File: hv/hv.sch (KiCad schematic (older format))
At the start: 26 parts, among them P1 CONN_02X03, P10 CONN_01X01, P2 CONN_01X02, P3 CONN_01X01, P4 CONN_01X01, P5 CONN_01X01, P6 CONN_01X02, P7 CONN_01X01, P8 CONN_01X01, P9 CONN_01X01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

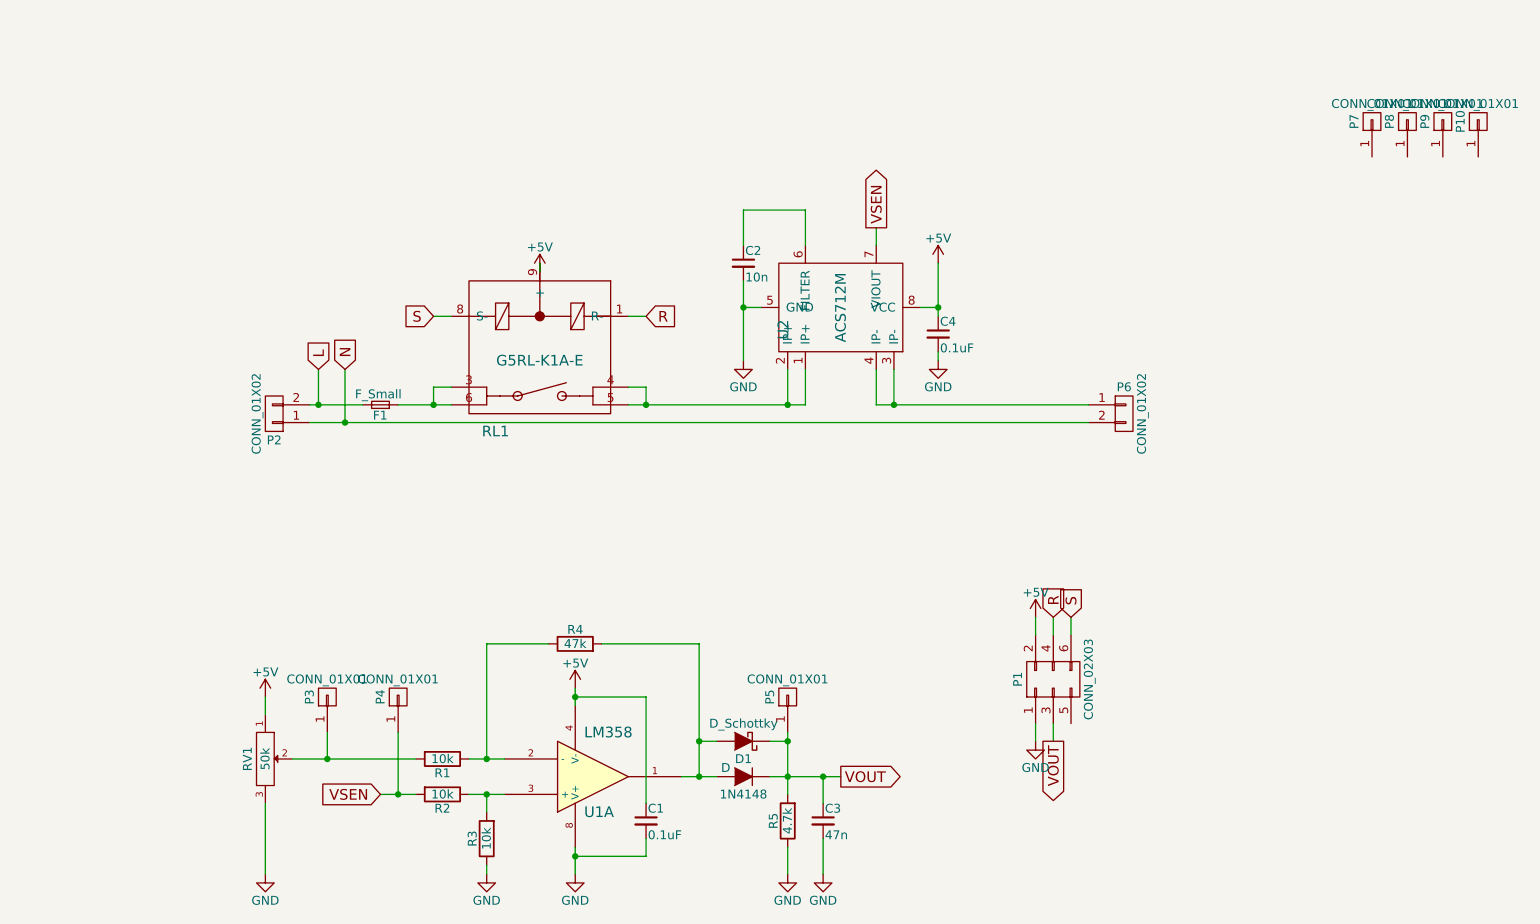
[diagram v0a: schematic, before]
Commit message: Rerouting on 5x5 cm2
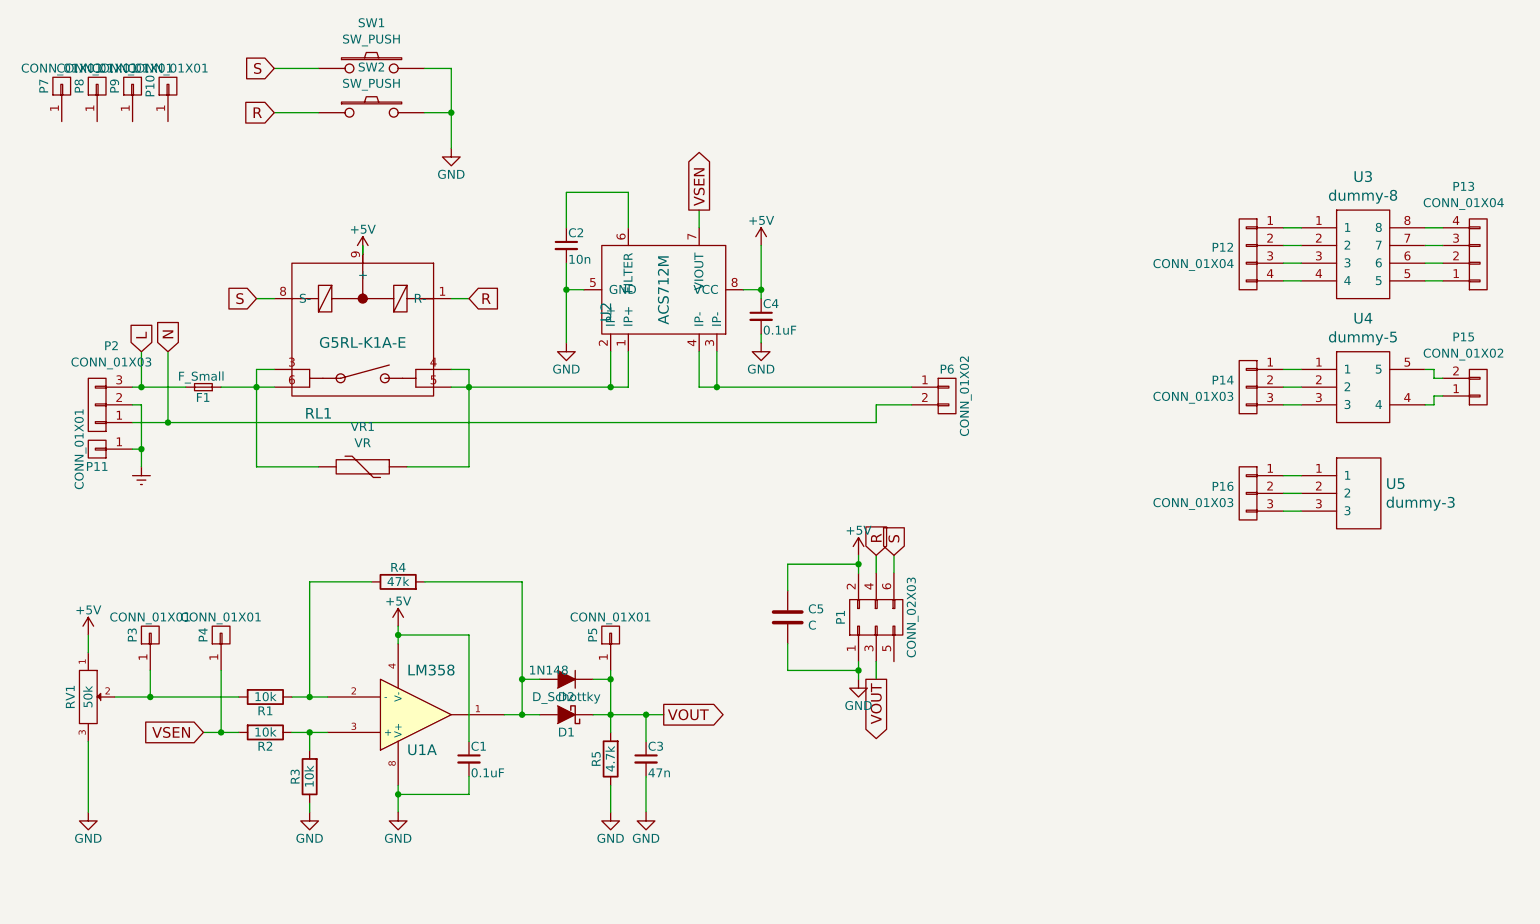
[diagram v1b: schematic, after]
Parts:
- removed P2: CONN_01X02, Connect:bornier2, symbol CONN_01X02
- added C5: C, Capacitors_SMD:C_0805, symbol C
- added P11: CONN_01X01, Pin_Headers:Pin_Header_Straight_1x01, symbol CONN_01X01
- added P12, P13: CONN_01X04, Pin_Headers:Pin_Header_Straight_1x04, symbol CONN_01X04
- added P14, P16: CONN_01X03, Pin_Headers:Pin_Header_Straight_1x03, symbol CONN_01X03
- added P15: CONN_01X02, Pin_Headers:Pin_Header_Straight_1x02, symbol CONN_01X02
- added P2: CONN_01X03, Connect:bornier3, symbol CONN_01X03
- added SW1, SW2: SW_PUSH, Buttons_Switches_ThroughHole:SW_PUSH_SMALL, symbol SW_PUSH
- added U3: dummy-8, SMD:SOIC_08_4.0mm_5.0mm_1.27mm, symbol dummy-8
- added U4: dummy-5, SMD:SOT-23-5, symbol dummy-5
- added U5: dummy-3, SMD:SOT-23-3, symbol dummy-3
- added VR1: VR, Varistors:RV_Disc_D12_W3.9_P7.5, symbol VR
- C1, C2, C3, C4: footprint Capacitors_SMD:C_0805_HandSoldering -> Capacitors_SMD:C_0805
- D2: renamed from 1N4148; value D -> 1N148
- R1, R2, R3, R4, R5: footprint Resistors_SMD:R_0805_HandSoldering -> Resistors_SMD:R_0805
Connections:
- net +5V: now also C5.1
- net GND: now also C5.2, SW1.2, SW2.2
- net L: now also P2.3 (P3)
- net N: now also P2.1 (P1)
- net R: now also SW2.1
- net S: now also SW1.1
- net at F1.1, RL1.3, RL1.6: now also VR1.2
- net at RL1.4, RL1.5, U2.1 (IP+)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: now also VR1.1
- new net: P12.1 (P1), U3.1
- new net: P12.2 (P2), U3.2
- new net: P12.3 (P3), U3.3
- new net: P12.4 (P4), U3.4
- new net: P13.1 (P1), U3.5
- new net: P13.2 (P2), U3.6
- new net: P13.3 (P3), U3.7
- new net: P13.4 (P4), U3.8
- new net: P14.1 (P1), U4.1
- new net: P14.2 (P2), U4.2
- new net: P14.3 (P3), U4.3
- new net: P15.1 (P1), U4.4
- new net: P15.2 (P2), U4.5
- new net: P16.1 (P1), U5.1
- new net: P16.2 (P2), U5.2
- new net: P16.3 (P3), U5.3
- new net Earth: P11.1 (P1), P2.2 (P2)
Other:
- moved on the sheet: C1, C2, C3, C4, D1, D2, F1, P1, P10, P3, P4, P5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
